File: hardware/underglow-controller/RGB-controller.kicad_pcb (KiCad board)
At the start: 4 copper layers, 86 x 74.9 mm, 171 parts, among them J2 U.FL-R-SMT-1(10), J3 U.FL-R-SMT-1(10), J4 CONSOLE, J5 U.FL-R-SMT-1(10), J6 DTM1312PA12PBR008, J7 Conn_01x04, J8 Conn_01x05, Q2 STS8DNF3LL, Q3 STS8DNF3LL, Q4 MBT3904DW1T1G, Q5 MBT3904DW1T1G, Q6 Q_PMOS_GDS, SW2 USB BOOT, SW3 SW_Push, SW4 SW_Push, SW5 SW_Push, U2 W25Q128JVS, U3 RP2040, U4 SX1231HIMLTRT, U5 ESP32-S3R2, U6 W25Q128JVS, U7 DRV8844PWP, U8 ADP2303ARDZ-3.3, U9 SN65HVD230, Y2 12MHZ, Y3 32mhz, Y4 40MHZ

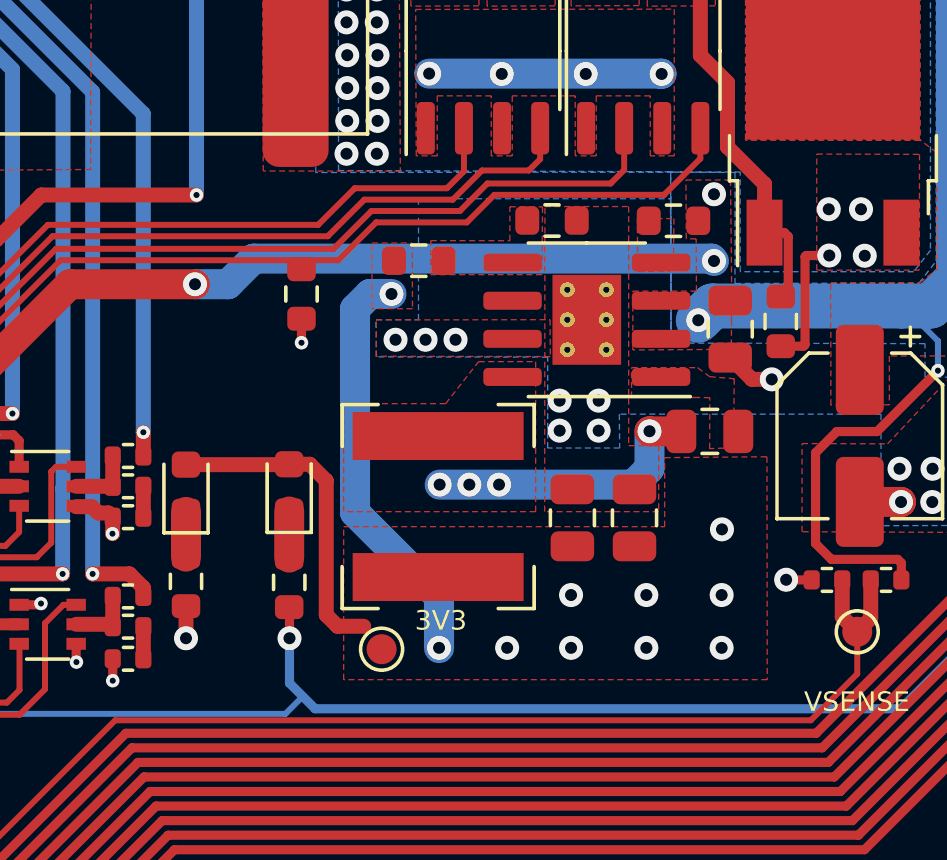
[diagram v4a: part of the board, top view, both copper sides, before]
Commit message: replace pmic
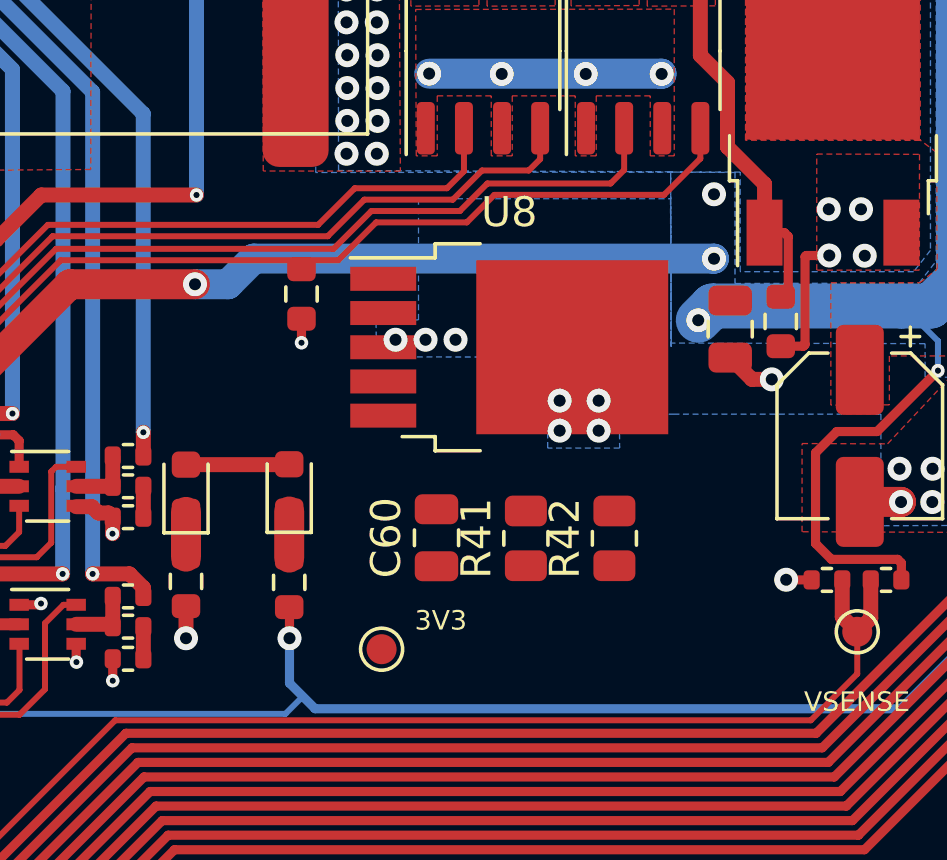
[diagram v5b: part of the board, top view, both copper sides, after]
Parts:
- removed the C59 at (83.0, 70.3)
- removed the C61 at (78.4, 73.2)
- removed L12: 4.7uH, Inductor_SMD:L_Bourns-SRN6028
- removed the R43 at (73.3, 64.6)
- removed the R44 at (77.7, 63.3)
- added R41: 56.7k, Resistor_SMD:R_0805_2012Metric, F.Cu at (76.9, 73.9)
- C59: renamed from C62; value 10uF -> 1uF
- C60: value 22uF -> 1uF
- R42: footprint Resistor_SMD:R_0603_1608Metric -> Resistor_SMD:R_0805_2012Metric
- U8: value ADP2303ARDZ-3.3 -> BD33C0AWFP-CE2; footprint Package_SO:SOIC-8-1EP_3.9x4.9mm_P1.27mm_EP2.29x3mm_ThermalVias -> Package_TO_SOT_SMD:TO-252-5_TabPin6
- moved R42 10.8 mm to (79.8, 73.9), turned to 90 degrees
- moved C60 6.63 mm to (73.9, 73.9)
- moved U8 2.74 mm to (76.3, 67.5), turned to 0 degrees
- renumbered C63 to C61, C65 to C62, C64 to C63, D11 to D10, D5 to D4, D6 to D5, D7 to D6, D8 to D7, D9 to D8, D10 to D9, R38 to R37, R39 to R38, R40 to R39, R41 to R40, R45 to R43, R46 to R44, R47 to R45, R48 to R46
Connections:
- C60 pad 1: +3V3 -> Net-(C60-Pad1)
- C60 pad 2: GND -> +3V3
- R42 pad 1: /VIN -> Net-(R41-Pad1)
- R42 pad 2: /Power/PGOOD -> GND
- U8 pad 1: /Power/BST -> /VIN
- U8 pad 2: /VIN -> /Power/IGN
- U8 pad 3: /VIN -> unconnected-(U8-Pad3)
- U8 pad 4: /Power/PGOOD -> Net-(C60-Pad1)
- U8 pad 5: /Power/FB -> Net-(R41-Pad1)
- U8 pad 6: unconnected-(U8-Pad6) -> GND
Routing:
- net +3V3: track 136.4 -> 115.2 mm, vias 37 -> 27
- net /Power/SW: track 9.43 -> 0.00 mm, vias 4 -> 0
- net unconnected-(U8-Pad3): vias 0 -> 2
- net GND: vias 194 -> 192
- removed copper zone on F.Cu, net +3V3
- removed copper zone on F.Cu, net /Power/BST
- removed copper zone on F.Cu, net /Power/FB
- removed copper zone on F.Cu, net /Power/PGOOD
- removed copper zone on F.Cu, net /Power/SW
- removed copper zone on F.Cu, net /VIN

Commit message: iasdf
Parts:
- removed AE2, AE3: Antenna_Shield, RF_Antenna:Texas_SWRA416_868MHz_915MHz
- removed AE4: PCB_ANT, RF_Antenna:Texas_SWRA117D_2.4GHz_Right
- removed C10, C13, C2, C3, C4, C5, C50, C6, C7, C8, C9: 0.1uF, Capacitor_SMD:C_0402_1005Metric
- removed C11, C12: 1uF, Capacitor_SMD:C_0402_1005Metric
- removed C14, C15: 20pF, Capacitor_SMD:C_0402_1005Metric
- removed C42, C56, C61, C62: 10uF, Capacitor_SMD:C_0805_2012Metric
- removed C54: 0.01uF, Capacitor_SMD:C_0805_2012Metric
- removed C55: 0.1uF, Capacitor_SMD:C_0805_2012Metric
- removed C57: 10uF, Capacitor_SMD:CP_Elec_5x5.3
- removed C58: 0.47uF, Capacitor_SMD:C_0805_2012Metric
- removed C59: 1uF, Capacitor_SMD:C_0805_2012Metric
- removed D10, D9: PESD2CANFD24V-T, Package_TO_SOT_SMD:SOT-23
- removed D2, D4, D5: GRN, LED_SMD:LED_0603_1608Metric
- removed D3: RED, LED_SMD:LED_0603_1608Metric
- removed D6, D7, D8: D_Small, Diode_SMD:D_SOD-123F
- removed F2: Fuse, ConeCodes:Keystone-3587-10TR
- removed J2: U.FL-R-SMT-1(10), ConeCodes:HRS_U.FL-R-SMT-1(10)
- removed J7: Conn_01x04, Connector_PinHeader_1.27mm:PinHeader_1x04_P1.27mm_Vertical
- removed Q4, Q5: MBT3904DW1T1G, Package_TO_SOT_SMD:SOT-363_SC-70-6
- removed Q6: Q_PMOS_GDS, Package_TO_SOT_SMD:TO-252-2
- removed R15, R16: 0R, Resistor_SMD:R_0402_1005Metric
- removed R18, R4: 100k, Resistor_SMD:R_0402_1005Metric
- removed R2, R3: 27r4, Resistor_SMD:R_0402_1005Metric
- removed R23, R38, R44: 10k, Resistor_SMD:R_0603_1608Metric
- removed R24: 0R, Resistor_SMD:R_2512_6332Metric
- removed R25, R26, R31, R32, R40, R8: 10k, Resistor_SMD:R_0402_1005Metric
- removed R27, R28, R33, R34, R46, R5: 1k, Resistor_SMD:R_0402_1005Metric
- removed R29, R30, R35, R36: 499R, Resistor_SMD:R_0402_1005Metric
- removed R37, R43, R6, R7: 240R, Resistor_SMD:R_0603_1608Metric
- removed R39: 36k, Resistor_SMD:R_0402_1005Metric
- removed R45: 120,DNF, Resistor_SMD:R_0805_2012Metric
- removed SW2: USB BOOT, ConeCodes:SW_RS-032G05A3-SMRT
- removed SW3: SW_Push, ConeCodes:SW_RS-032G05A3-SMRT
- removed TP8: VSENSE, TestPoint:TestPoint_Pad_D1.0mm
- removed TP9: 3V3OUT, TestPoint:TestPoint_Pad_D1.0mm
- removed U2: W25Q128JVS, Package_SO:SOIC-8W_5.3x5.3mm_P1.27mm
- removed U3: RP2040, ConeCodes:QFN-56
- removed U7: DRV8844PWP, Package_SO:HTSSOP-28-1EP_4.4x9.7mm_P0.65mm_EP2.85x5.4mm_ThermalVias
- removed U9: SN65HVD230, Package_SO:SOIC-8_3.9x4.9mm_P1.27mm
- removed Y2: 12MHZ, Crystal:Crystal_SMD_3225-4Pin_3.2x2.5mm
- added Q7: STS8DNF3LL, Package_SO:SO-8_3.9x4.9mm_P1.27mm, F.Cu at (37.2, 63.1)
- added Q8: STS8DNF3LL, Package_SO:SO-8_3.9x4.9mm_P1.27mm, F.Cu at (68.8, 74.5)
- added REF**: VQFN-48-1EP_7x7mm_P0.5mm_EP5.15x5.15mm_ThermalVias, Package_DFN_QFN:VQFN-48-1EP_7x7mm_P0.5mm_EP5.15x5.15mm_ThermalVias, F.Cu at (39.1, 76.3)
- J6: value DTM1312PA12PBR008 -> Delphi_Sicma_24; footprint ConeCodes:TE_DTM1312PA12PBR008 -> ConeCodes:Delphi_Sicma_24_Black
- moved G*** 44.6 mm to (37.0, 129.1)
- moved Q3 25.6 mm to (61.4, 74.3)
- moved Q2 25.6 mm to (56.0, 74.3)
- moved C60 20.4 mm to (94.0, 70.7), turned to 180 degrees
- moved R41 18.2 mm to (94.0, 67.7), turned to 180 degrees
- moved R42 16.9 mm to (94.0, 64.8), turned to 180 degrees
- moved C21 12.1 mm to (90.6, 108.9)
- moved C22 12.1 mm to (84.7, 109.4)
- moved C27 12.1 mm to (79.9, 105.3)
- moved C28 12.1 mm to (80.9, 105.3)
- moved C30 12.1 mm to (86.1, 112.5)
- moved C32 12.1 mm to (85.2, 113.6)
- moved C33 12.1 mm to (87.6, 112.5)
- moved C34 12.1 mm to (90.6, 112.5)
- moved C35 12.1 mm to (84.7, 112.1)
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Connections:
- net /External-IO/VOUT_EN renamed /External-IO/GPIO4
- J6 pad A1: /Connectors/GPO1 -> unconnected-(J6-PadA1)
- J6 pad A2: /Connectors/GPO2 -> unconnected-(J6-PadA2)
- J6 pad A3: /Connectors/GPO3 -> unconnected-(J6-PadA3)
- J6 pad A4: /Connectors/LEDA -> unconnected-(J6-PadA4)
- J6 pad A5: GND -> unconnected-(J6-PadA5)
- J6 pad A6: /Connectors/IGNITION -> unconnected-(J6-PadA6)
- J6 pad A7: /Connectors/MOTOR1_OUT1 -> unconnected-(J6-PadA7)
- J6 pad A8: /Connectors/MOTOR1_OUT2 -> unconnected-(J6-PadA8)
- J6 pad B1: /CAN_P -> unconnected-(J6-PadB1)
- J6 pad B2: /Connectors/GPI2 -> unconnected-(J6-PadB2)
- J6 pad B3: /Connectors/GPI4 -> unconnected-(J6-PadB3)
- J6 pad B4: /Connectors/USB_D_P -> unconnected-(J6-PadB4)
- J6 pad B5: /Connectors/USB_D_N -> unconnected-(J6-PadB5)
- J6 pad B6: GND -> unconnected-(J6-PadB6)
- J6 pad B7: Net-(D6-Pad2) -> unconnected-(J6-PadB7)
- R10 pad 2: Net-(J2-Pad2) -> unconnected-(R10-Pad2)
- R11 pad 1: Net-(AE3-Pad1) -> unconnected-(R11-Pad1)
- R17 pad 1: Net-(AE4-Pad1) -> unconnected-(R17-Pad1)
- R9 pad 1: Net-(AE2-Pad1) -> unconnected-(R9-Pad1)
- U5 pad 10: /MCPWM0_INB -> /ESP32-S3/GPIO5
- U5 pad 11: /MCPWM0_ENB -> /ESP32-S3/GPIO6
- U5 pad 12: /MCPWM1_INA -> /ESP32-S3/GPIO7
- U5 pad 13: /MCPWM1_ENA -> /ESP32-S3/GPIO8
- U5 pad 15: /MCPWM1_INB -> /ESP32-S3/GPIO10
- U5 pad 16: /MCPWM1_ENB -> /ESP32-S3/GPIO11
- U5 pad 17: /MCPWM_SLEEP -> /ESP32-S3/GPIO12
- U5 pad 28: /MCPWM_FAULT -> /ESP32-S3/SPICS1
- U5 pad 8: /MCPWM0_INA -> /ESP32-S3/GPIO3
- U5 pad 9: /MCPWM0_ENA -> /ESP32-S3/GPIO4
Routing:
- net /VIN: track 82.5 -> 0.00 mm, vias 8 -> 0
- net /MCPWM0_INA: track 69.2 -> 0.00 mm
- net /MCPWM_FAULT: track 68.3 -> 0.00 mm, vias 3 -> 0
- net /MCPWM0_ENA: track 67.8 -> 0.00 mm
- net /MCPWM0_INB: track 66.7 -> 0.00 mm
- net /MCPWM0_ENB: track 65.5 -> 0.00 mm
- net /MCPWM1_INA: track 64.2 -> 0.00 mm
- net /MCPWM1_ENA: track 63.2 -> 0.00 mm
- net /MCPWM1_ENB: track 60.8 -> 0.00 mm
- net /MCPWM1_INB: track 60.6 -> 0.00 mm
- net /MCPWM_SLEEP: track 58.7 -> 0.00 mm
- net GND: track 225.8 -> 167.9 mm, vias 192 -> 138
- net /Connectors/LEDA: track 55.8 -> 0.00 mm, vias 1 -> 0
- net /MISO: track 122.8 -> 69.0 mm, vias 4 -> 2
- net /MOSI: track 118.0 -> 66.1 mm
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- removed copper zone on B.Cu, net /Connectors/FUSE_IN
- removed copper zone on F.Cu, net /Connectors/FUSE_IN
- removed copper zone on B.Cu, net /Connectors/FUSE_OUT
- removed copper zone on F.Cu, net /Connectors/FUSE_OUT
- removed copper zone on F.Cu, net /Connectors/GPO1
- removed copper zone on F.Cu, net /Connectors/GPO2
- removed copper zone on F.Cu, net /Connectors/GPO3
- removed copper zone on F.Cu, net /Connectors/MOTOR1_OUT1
- removed copper zone on F.Cu, net /Connectors/MOTOR1_OUT2
- removed copper zone on F.Cu, net /Connectors/MOTOR2_OUT1
- removed copper zone on F.Cu, net /Connectors/MOTOR2_OUT2
- removed copper zone on B.Cu, net /Connectors/VOUT
- removed copper zone on F.Cu, net /Connectors/VOUT
- removed copper zone on In2.Cu, net /Connectors/VOUT
- removed copper zone on F.Cu, net /External-IO/GPIO4
- removed copper zone on B.Cu, net /VIN
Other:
- board size 86 x 74.9 mm -> 78.5 x 93 mm
- board text removed: "3V3"
- board text removed: "BLUE"
- board text removed: "CAN H"
- board text removed: "CAN L"
- board text removed: "CONSOLE"
- board text removed: "D+"
- board text removed: "D-"
- board text removed: "GPI1"
- board text removed: "GPI2"
- board text removed: "GPI3"
- board text removed: "GPI4"
- board text removed: "GREEN"
- board text removed: "IGN"
- board text removed: "JLCJLCJLCJLC"
- board text removed: "MOTOR1 A"
- board text removed: "MOTOR1 B"
- board text removed: "MOTOR2 A"
- board text removed: "MOTOR2 B"
- board text removed: "RED"
- board text removed: "Reset"
- board text removed: "USB BOOT"
- board text removed: "USB D+"
- board text removed: "USB D-"
- board text removed: "VBATT"
- board text removed: "VIN"
- board text removed: "VOUT"
- board text removed: "VSENSE"

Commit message: schematic rework progress
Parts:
- removed REF**: VQFN-48-1EP_7x7mm_P0.5mm_EP5.15x5.15mm_ThermalVias, Package_DFN_QFN:VQFN-48-1EP_7x7mm_P0.5mm_EP5.15x5.15mm_ThermalVias
- added C28: 10uF, Capacitor_SMD:C_0805_2012Metric, F.Cu at (100.4, 72.7)
- added C36: 0.1uF, Capacitor_SMD:C_0402_1005Metric, F.Cu at (98.9, 77.8)
- added C40: C_Small, Capacitor_SMD:C_0805_2012Metric, F.Cu at (53.4, 70.0)
- added C41: C_Small, Capacitor_SMD:C_0805_2012Metric, F.Cu at (55.6, 70.0)
- added C42: CIN2, Capacitor_SMD:C_0805_2012Metric, F.Cu at (35.1, 80.7)
- added C43: C_Small, Capacitor_SMD:C_0805_2012Metric, F.Cu at (60.3, 77.7)
- added C44: CBST1, Capacitor_SMD:C_0805_2012Metric, F.Cu at (46.9, 76.8)
- added C45: COUT11, Capacitor_SMD:C_0805_2012Metric, F.Cu at (47.9, 70.0)
- added C46: COUT12, Capacitor_SMD:C_0805_2012Metric, F.Cu at (45.8, 70.0)
- added C47: COUT13, Capacitor_SMD:C_1206_3216Metric, F.Cu at (37.0, 53.3)
- added C48: CCOMP1, Capacitor_SMD:C_0805_2012Metric, F.Cu at (97.1, 82.5)
- added C49: CSOFT_START1, Capacitor_SMD:C_0805_2012Metric, F.Cu at (78.3, 94.1)
- added C50: CCOMP2, Capacitor_SMD:C_0805_2012Metric, F.Cu at (59.5, 83.8)
- added C51: CSOFT_START2, Capacitor_SMD:C_0805_2012Metric, F.Cu at (56.0, 84.7)
- added C52: CIN3, Capacitor_SMD:C_0805_2012Metric, F.Cu at (35.2, 75.0)
- added C53: CBST2, Capacitor_SMD:C_0805_2012Metric, F.Cu at (46.9, 80.3)
- added C54: COUT21, Capacitor_SMD:C_0805_2012Metric, F.Cu at (50.7, 84.4)
- added C55: COUT22, Capacitor_SMD:C_0805_2012Metric, F.Cu at (48.7, 84.4)
- added C56: COUT23, Capacitor_SMD:C_1206_3216Metric, F.Cu at (37.0, 50.7)
- added C57: 1uF, Capacitor_SMD:C_0805_2012Metric, F.Cu at (99.4, 68.1)
- added C59: 10uF, Capacitor_SMD:C_0805_2012Metric, F.Cu at (73.5, 94.1)
- added C60: 10uF, Capacitor_SMD:C_0805_2012Metric, F.Cu at (83.5, 72.5)
- added D2: D_Schottky_Small, Diode_SMD:D_SOD-523, F.Cu at (47.4, 75.0)
- added D3: D_Schottky_Small, Diode_SMD:D_SOD-523, F.Cu at (47.4, 78.5)
- added D4: GRN, LED_SMD:LED_0603_1608Metric, F.Cu at (84.2, 94.1)
- added D5: D_Small, Diode_SMD:D_SOD-123F, F.Cu at (83.8, 88.2)
- added D6: D_Small, Diode_SMD:D_SOD-123F, F.Cu at (82.9, 75.6)
- added D8: PESD2CANFD24V-T, Package_TO_SOT_SMD:SOT-23, F.Cu at (71.1, 78.7)
- added D9: PESD2CANFD24V-T, Package_TO_SOT_SMD:SOT-23, F.Cu at (76.8, 78.9)
- added L12: L_Small, ConeCodes:SRP1265A-100M, F.Cu at (37.1, 64.3)
- added L13: L_Small, ConeCodes:SRP1265A-100M, F.Cu at (37.0, 89.6)
- added Q6: STS8DNF3LL, Package_SO:SO-8_3.9x4.9mm_P1.27mm, F.Cu at (40.0, 79.4)
- added Q7: MBT3904DW1T1G, Package_TO_SOT_SMD:SOT-363_SC-70-6, F.Cu at (90.7, 80.2)
- added Q8: MBT3904DW1T1G, Package_TO_SOT_SMD:SOT-363_SC-70-6, F.Cu at (82.6, 84.2)
- added R11: 100k, Resistor_SMD:R_0402_1005Metric, F.Cu at (100.9, 76.4)
- added R16: RFB1, Resistor_SMD:R_0805_2012Metric, F.Cu at (31.4, 73.4)
- added R17: RVBH1, Resistor_SMD:R_0603_1608Metric, F.Cu at (49.7, 70.0)
- added R18: RFREQ, Resistor_SMD:R_0402_1005Metric, F.Cu at (66.1, 83.9)
- added R19: RVBL1, Resistor_SMD:R_0603_1608Metric, F.Cu at (51.2, 70.0)
- added R21: RCOMP1, Resistor_SMD:R_0402_1005Metric, F.Cu at (63.2, 83.9)
- added R22: RCOMP1, Resistor_SMD:R_0402_1005Metric, F.Cu at (63.2, 85.9)
- added R23: 10k, Resistor_SMD:R_0402_1005Metric, F.Cu at (78.9, 86.1)
- added R24: 10k, Resistor_SMD:R_0402_1005Metric, F.Cu at (81.8, 79.8)
- added R25: RFB2, Resistor_SMD:R_0805_2012Metric, F.Cu at (31.3, 80.2)
- added R26: RVBH2, Resistor_SMD:R_0603_1608Metric, F.Cu at (52.6, 84.4)
- added R27: 1k, Resistor_SMD:R_0402_1005Metric, F.Cu at (87.8, 81.9)
- added R28: 1k, Resistor_SMD:R_0402_1005Metric, F.Cu at (89.0, 77.3)
- added R29: 499R, Resistor_SMD:R_0402_1005Metric, F.Cu at (84.7, 79.8)
- added R30: 499R, Resistor_SMD:R_0402_1005Metric, F.Cu at (94.8, 78.1)
- added R31: RVBL2, Resistor_SMD:R_0603_1608Metric, F.Cu at (54.2, 84.4)
- added R33: 10k, Resistor_SMD:R_0402_1005Metric, F.Cu at (94.8, 76.1)
- added R34: 10k, Resistor_SMD:R_0402_1005Metric, F.Cu at (84.7, 77.8)
- added R35: 1k, Resistor_SMD:R_0402_1005Metric, F.Cu at (91.9, 75.3)
- added R36: 1k, Resistor_SMD:R_0402_1005Metric, F.Cu at (95.5, 72.1)
- added R37: 499R, Resistor_SMD:R_0402_1005Metric, F.Cu at (94.8, 74.2)
- added R38: 499R, Resistor_SMD:R_0402_1005Metric, F.Cu at (91.9, 77.3)
- added R39: 0R, Resistor_SMD:R_2512_6332Metric, F.Cu at (95.0, 89.8)
- added R40: 36k, Resistor_SMD:R_0402_1005Metric, F.Cu at (95.4, 70.3)
- added R41: 10k, Resistor_SMD:R_0402_1005Metric, F.Cu at (81.8, 91.3)
- added R44: 240R, Resistor_SMD:R_0603_1608Metric, F.Cu at (95.2, 68.3)
- added R45: 120,DNF, Resistor_SMD:R_0805_2012Metric, F.Cu at (80.3, 68.0)
- added R46: 1k, Resistor_SMD:R_0402_1005Metric, F.Cu at (85.1, 62.0)
- added R8: 0R, Resistor_SMD:R_0402_1005Metric, F.Cu at (97.9, 74.9)
- added R9: 0R, Resistor_SMD:R_0402_1005Metric, F.Cu at (97.9, 72.0)
- added TP8: VSENSE, TestPoint:TestPoint_Pad_D1.0mm, F.Cu at (80.7, 93.8)
- added TP9: 3V3OUT, TestPoint:TestPoint_Pad_D1.0mm, F.Cu at (84.7, 91.2)
- added U5: TLD55012QVXUMA1, Package_DFN_QFN:VQFN-48-1EP_7x7mm_P0.5mm_EP5.15x5.15mm_ThermalVias, F.Cu at (54.1, 77.0)
- added U7: SN65HVD230, Package_SO:SOIC-8_3.9x4.9mm_P1.27mm, F.Cu at (89.0, 70.6)
- moved R42 12.1 mm to (99.4, 56.9)
- moved R43 12.1 mm to (99.4, 53.9)
- moved C58 12.1 mm to (99.4, 59.8)
- moved U6 12.1 mm to (93.0, 57.4)
- moved Q5 10.7 mm to (40.1, 73.5), turned to 180 degrees
- moved Q3 7.39 mm to (66.8, 69.3)
- moved Q2 7.20 mm to (61.2, 69.3)
- moved Q4 6.28 mm to (72.4, 69.3)
- renumbered C24 to C10, C25 to C11, C26 to C12, C27 to C13, C28 to C14, C29 to C15, C30 to C16, C31 to C17, C32 to C18, C33 to C19, C16 to C2, C34 to C20, C35 to C21, C36 to C22, C37 to C23, C38 to C24, C39 to C25, C40 to C26, C41 to C27, C43 to C29, C17 to C3, C44 to C30, C45 to C31, C46 to C32, C47 to C33, C48 to C34, C49 to C35, C51 to C37, C52 to C38, C53 to C39, C18 to C4, C19 to C5, C60 to C58, C20 to C6, C63 to C61, C21 to C7, C22 to C8, C23 to C9, J3 to J2, J4 to J3, J5 to J4, J6 to J5, J8 to J7, Q8 to Q4, Q7 to Q5, R17 to R10, R19 to R12, R20 to R13, R21 to R14, R22 to R15, R9 to R2, R10 to R3, R11 to R4, R41 to R42, R42 to R43, R12 to R5, R13 to R6, R14 to R7, SW4 to SW2, SW5 to SW3, U4 to U2, U5 to U3, U6 to U4, U8 to U6, Y3 to Y2, Y4 to Y3
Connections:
- Q5 pad 1: GND -> /External-IO/SWN1
- Q5 pad 2: /GPIO_GPO1 -> /External-IO/HSGD1
- Q5 pad 3: GND -> /External-IO/SWCS1
- Q5 pad 4: /GPIO_GPO2 -> /External-IO/LSGD1
- Q5 pad 5: /Connectors/GPO2 -> /External-IO/SWN1
- Q5 pad 6: /Connectors/GPO2 -> /External-IO/SWN1
- Q5 pad 7: /Connectors/GPO1 -> /External-IO/VBAT
- Q5 pad 8: /Connectors/GPO1 -> /External-IO/VBAT
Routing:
- net /Connectors/GPO1: track 0.00 -> 4.48 mm
- net /Connectors/GPO3: track 0.00 -> 3.89 mm
- net /Connectors/GPO2: track 0.00 -> 3.76 mm
- net /External-IO/GPIO4: track 0.00 -> 3.53 mm
- net /External-IO/GPO5: track 0.00 -> 3.42 mm
- net /External-IO/GPO6: track 0.00 -> 3.10 mm
- net GND: vias 138 -> 137
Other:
- board text removed: "vout"
